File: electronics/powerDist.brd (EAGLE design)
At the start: 100 x 80 mm, 4 parts

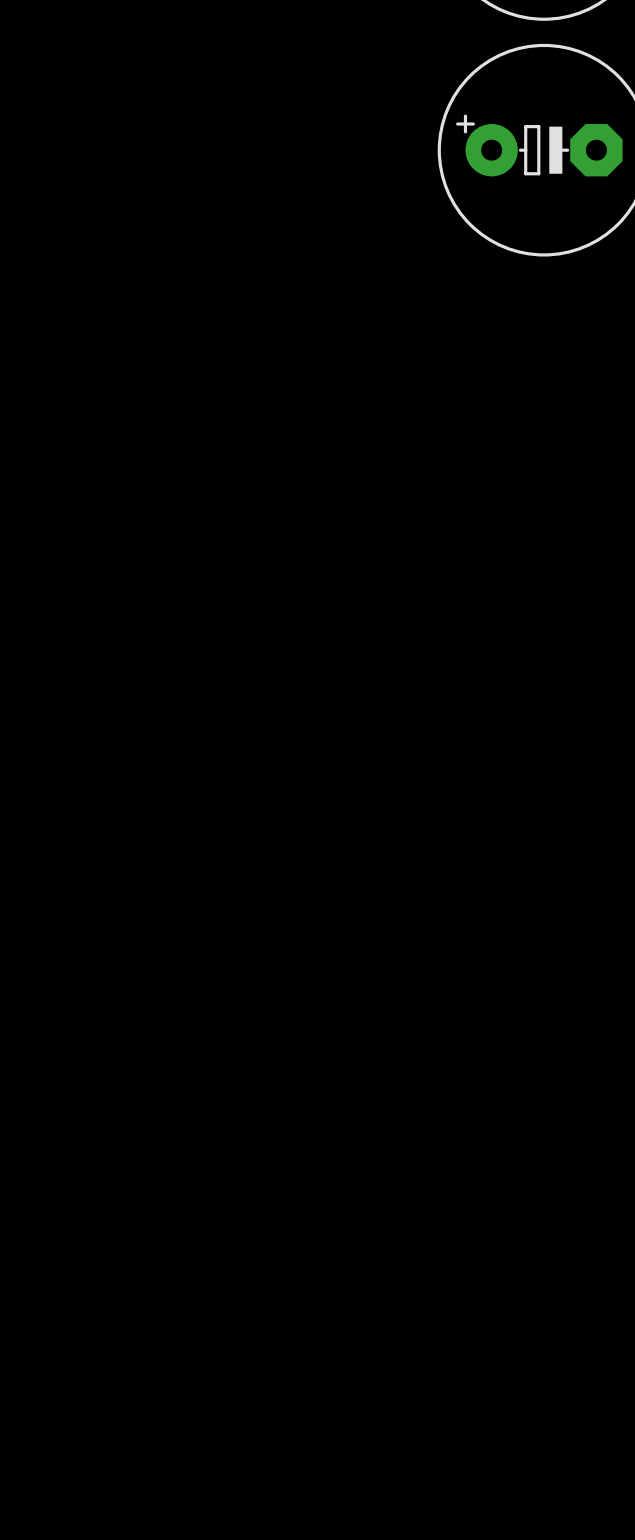
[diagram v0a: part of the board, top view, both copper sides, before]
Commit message: added msp430, went with drv ti motor drivers for galvos and brushed motor, max 1.8A
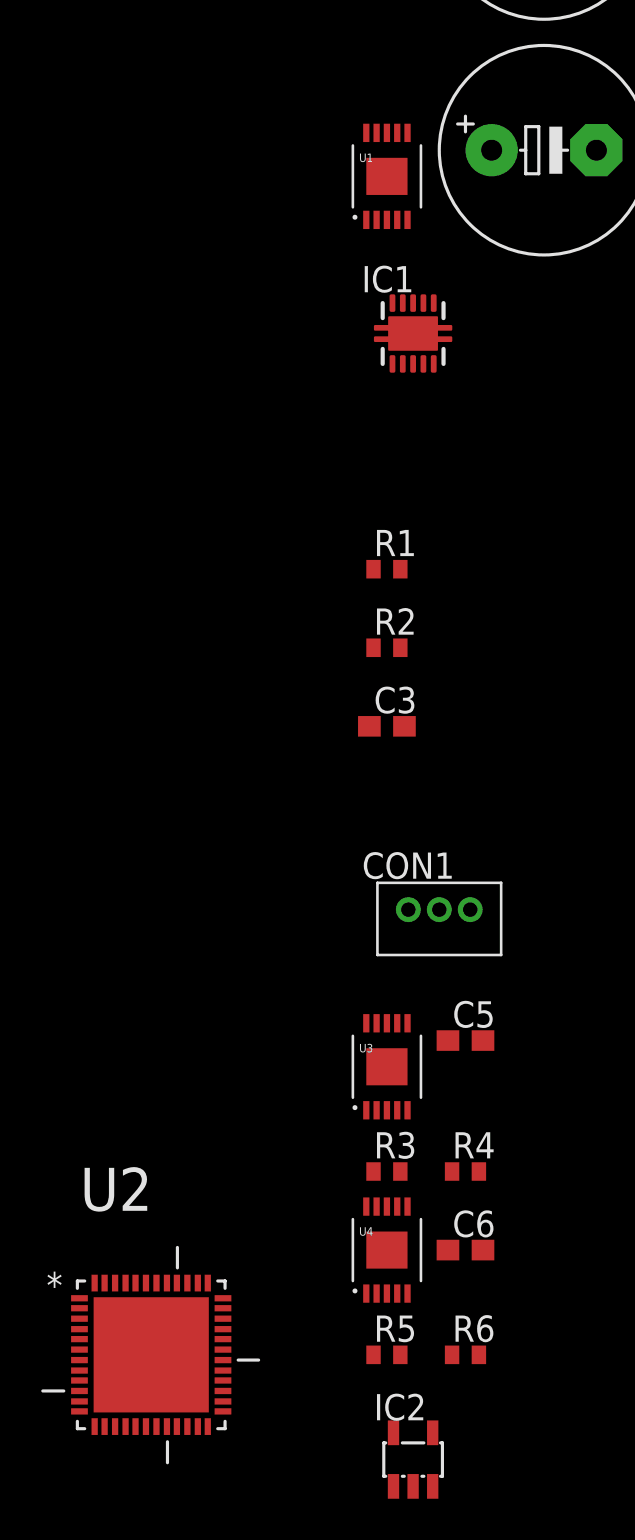
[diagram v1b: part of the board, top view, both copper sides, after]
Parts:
- added C3, C5, C6: (no value), rcl:C0603
- added CON1: B3B-ZR, jst:B3B-ZR
- added IC1: TPS6300, texas:DRC-S-PVSON-N10
- added IC2: TPS77033, texas:SOT23-DBV
- added R1, R2, R3, R4, R5, R6: (no value), rcl:R0402
- added U1, U3, U4: DRV8830, SparkFun-PowerIC:MSOP-10-GNDPAD
- added U2: MSP430F5500IRGZR, Texas Instruments_By_element14_Batch_1:QFN50P700X700X100-49N
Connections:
- new net +3V3: IC2.5
- new net +5V: C3.1, C5.1, C6.1, IC1.1, IC2.1, R1.2, R2.2, R3.2, R4.2, R5.2, R6.2, U1.4, U1.8, U3.4, U4.4, U4.7
- new net AVCC1: U2.7
- new net AVSS1: U2.10
- new net AVSS2: U2.44
- new net DRIVER_FAULT_1: U3.6
- new net DRIVER_FAULT_2: U4.6
- new net DRIVER_FAULT_3: U1.6
- new net DVCC1: U2.11
- new net DVCC2: U2.28
- new net DVSS1: U2.12
- new net DVSS2: U2.27
- new net MOTOR_SCL: R2.1, R4.1, R6.1, U1.10, U2.31, U3.10, U4.10
- new net MOTOR_SDA: R1.1, R3.1, R5.1, U1.9, U2.30, U3.9, U4.9
- new net OUT1: U1.3, U3.3, U4.3
- new net OUT2: U1.1, U3.1, U4.1
- new net PGND: IC1.3
- new net SAT_GND: CON1.2
- new net SAT_SERIAL: CON1.1, U2.34
- new net SAT_VCC: CON1.3
- new net V18: U2.43
- new net VCORE: U2.13
- new net VSSU: U2.37
- net GND: now also C3.2, C5.2, C6.2, IC1.9, IC2.2, IC2.3, U1.5, U1.7, U1.GND, U3.5, U3.7, U3.8, U3.GND, U4.5, U4.8, U4.GND

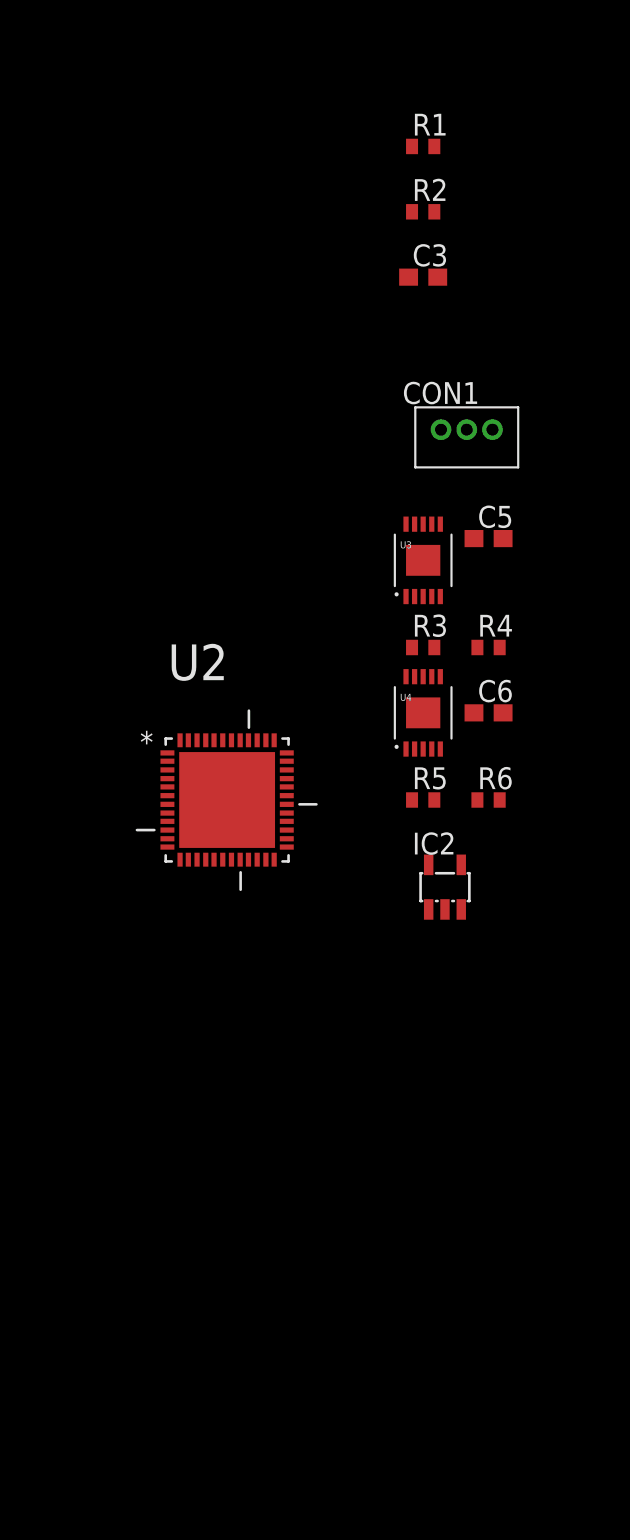
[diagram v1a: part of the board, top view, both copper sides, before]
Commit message: added passives to dc/dc.  todo figure out analog/micro stuff and connection points for motors
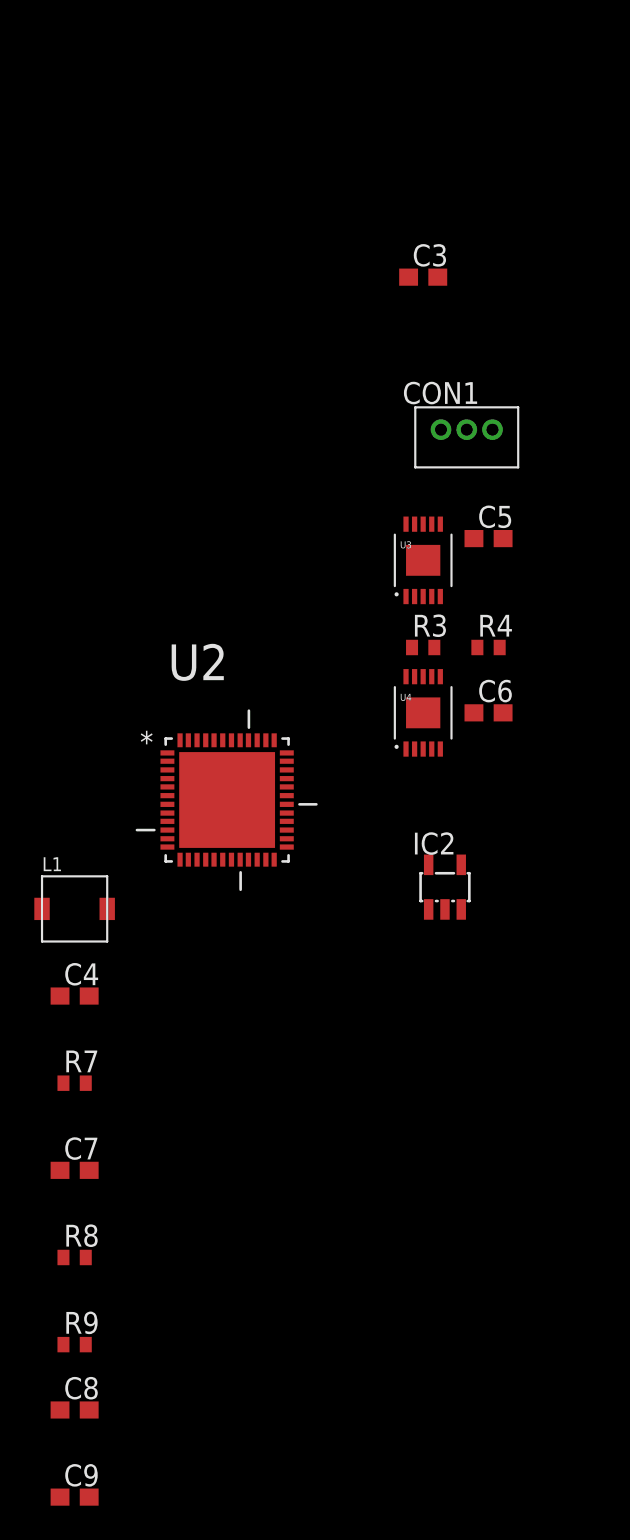
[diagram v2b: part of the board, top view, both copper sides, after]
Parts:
- removed R1, R2, R5, R6: (no value), rcl:R0402
- added C4: .1uf, rcl:C0603
- added C7, C8, C9: 10uf, rcl:C0603
- added L1: TDK-VLF4012AT-2R2M1R5, passives:TDK-VLF4012AT-2R2M1R5
- added R7: 100, rcl:R0402
- added R8, R9: (no value), rcl:R0402
- C3, C5, C6: value (none) -> .1uf
- R3, R4: value (none) -> 2k
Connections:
- removed net AVSS1: U2.10
- removed net AVSS2: U2.44
- removed net DVSS1: U2.12
- removed net DVSS2: U2.27
- removed net PGND: IC1.3
- removed net VSSU: U2.37
- new net N$3: IC1.4, L1.P$1
- new net N$4: IC1.2, L1.P$2
- new net N$8: C4.1, IC1.6, IC1.7, IC1.8, R7.1
- new net N$9: IC1.10, R8.1, R9.2
- net +5V: now also C8.1, C9.1, R8.2; no longer R1.2, R2.2, R5.2, R6.2
- net GND: now also C4.2, C7.2, C8.2, C9.2, IC1.3, R9.1, U2.10, U2.12, U2.27, U2.37, U2.44, U2.49
- net MOTOR_SCL: no longer R2.1, R6.1
- net MOTOR_SDA: no longer R1.1, R5.1
- net N$2: now also C7.1, IC1.5, R7.2

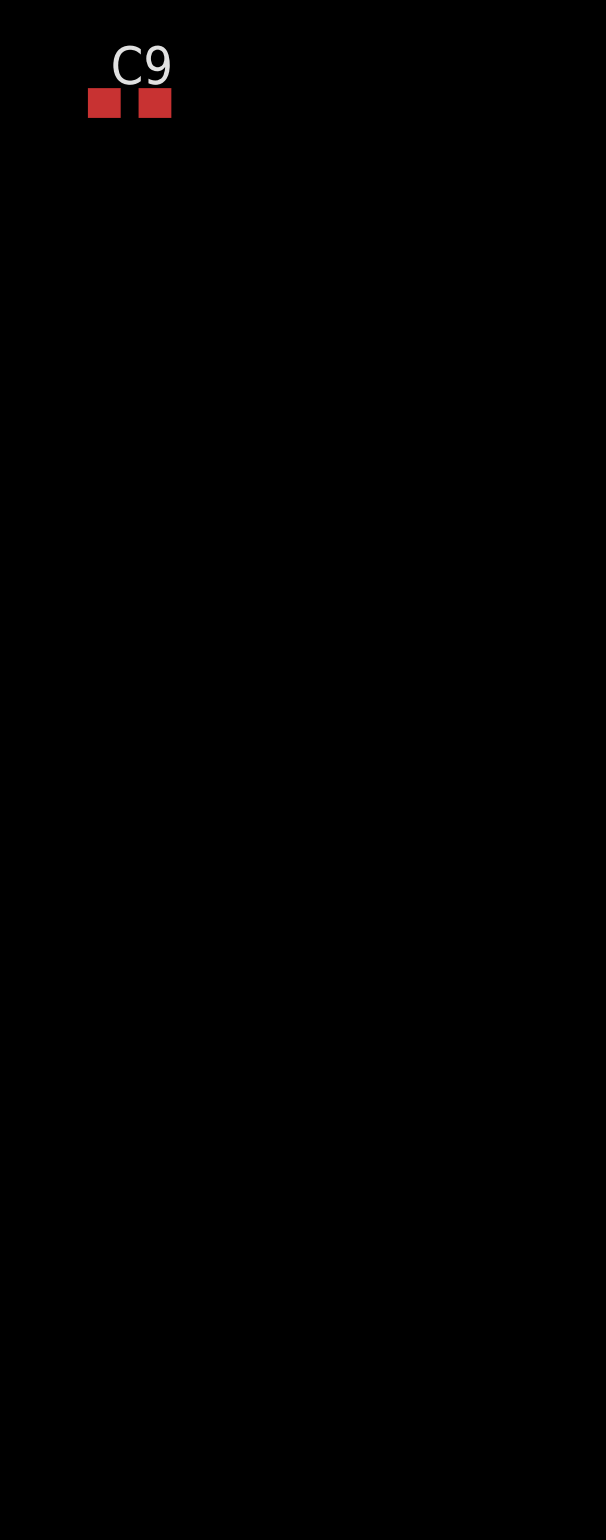
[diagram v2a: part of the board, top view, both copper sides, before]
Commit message: added decoupling to mcu
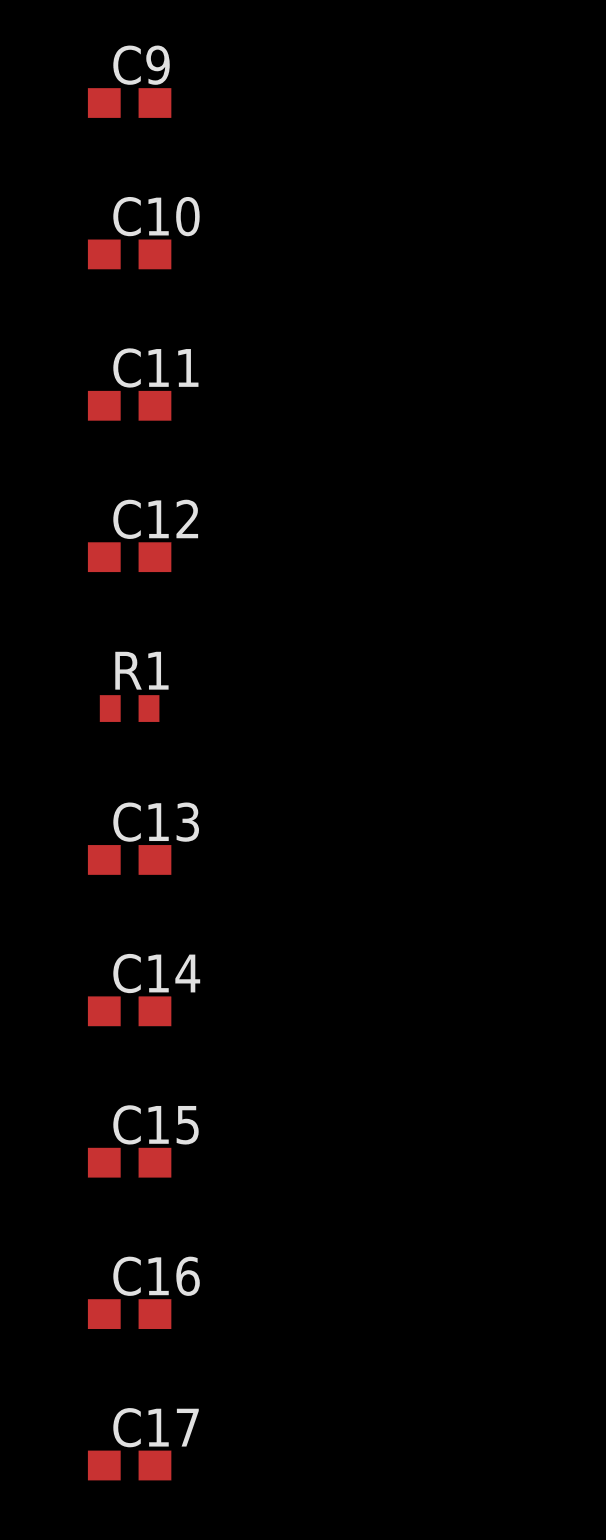
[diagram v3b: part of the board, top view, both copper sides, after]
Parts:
- added C10, C11, C12, C13: .1uf, rcl:C0603
- added C14, C15, C16, C17: 4.7uf, rcl:C0603
- added R1: 100, rcl:R0402
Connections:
- removed net AVCC1: U2.7
- removed net DVCC1: U2.11
- removed net DVCC2: U2.28
- removed net SAT_GND: CON1.2
- removed net SAT_VCC: CON1.3
- removed net VCORE: U2.13
- new net N$5: C13.1, C15.1, R1.2, U2.7
- new net N$7: C11.1, C14.1, U2.13
- net +3V3: now also C10.1, C12.1, C16.1, C17.1, CON1.3, R1.1, U2.11, U2.28
- net GND: now also C10.2, C11.2, C12.2, C13.2, C14.2, C15.2, C16.2, C17.2, CON1.2
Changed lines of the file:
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@@
 <element name="C8" library="rcl" package="C0603" value="10uf" x="-44.45" y="-111.76"/>
 <element name="C9" library="rcl" package="C0603" value="10uf" x="-44.45" y="-116.84"/>
+<element name="C10" library="rcl" package="C0603" value=".1uf" x="-44.45" y="-121.92"/>
+<element name="C11" library="rcl" package="C0603" value=".1uf" x="-44.45" y="-127"/>
+<element name="C12" library="rcl" package="C0603" value=".1uf" x="-44.45" y="-132.08"/>
+<element name="R1" library="rcl" package="R0402" value="100" x="-44.45" y="-137.16"/>
+<element name="C13" library="rcl" package="C0603" value=".1uf" x="-44.45" y="-142.24"/>
+<element name="C14" library="rcl" package="C0603" value="4.7uf" x="-44.45" y="-147.32"/>
+<element name="C15" library="rcl" package="C0603" value="4.7uf" x="-44.45" y="-152.4"/>
+<element name="C16" library="rcl" package="C0603" value="4.7uf" x="-44.45" y="-157.48"/>
+<element name="C17" library="rcl" package="C0603" value="4.7uf" x="-44.45" y="-162.56"/>
 </elements>
 <signals>
@@
 <contactref element="U2" pad="37"/>
 <contactref element="U2" pad="49"/>
+<contactref element="C11" pad="2"/>
+<contactref element="C10" pad="2"/>
+<contactref element="C12" pad="2"/>
+<contactref element="C13" pad="2"/>
+<contactref element="CON1" pad="2"/>
+<contactref element="C14" pad="2"/>
+<contactref element="C17" pad="2"/>
+<contactref element="C16" pad="2"/>
+<contactref element="C15" pad="2"/>
+<wire x1="-43.6" y1="-157.48" x2="-43.6" y2="-162.56" width="0" layer="19" extent="1-1"/>
+<wire x1="-43.6" y1="-152.4" x2="-43.6" y2="-157.48" width="0" layer="19" extent="1-1"/>
+<wire x1="-43.6" y1="-147.32" x2="-43.6" y2="-152.4" width="0" layer="19" extent="1-1"/>
+<wire x1="-43.6" y1="-142.24" x2="-43.6" y2="-147.32" width="0" layer="19" extent="1-1"/>
+<wire x1="-43.6" y1="-132.08" x2="-43.6" y2="-142.24" width="0" layer="19" extent="1-1"/>
+<wire x1="-43.6" y1="-127" x2="-43.6" y2="-132.08" width="0" layer="19" extent="1-1"/>
+<wire x1="-43.6" y1="-121.92" x2="-43.6" y2="-127" width="0" layer="19" extent="1-1"/>
+<wire x1="-43.6" y1="-116.84" x2="-43.6" y2="-121.92" width="0" layer="19" extent="1-1"/>
 <wire x1="-43.6" y1="-111.76" x2="-43.6" y2="-116.84" width="0" layer="19" extent="1-1"/>
 <wire x1="-45.1" y1="-107.95" x2="-43.6" y2="-111.76" width="0" layer="19" extent="1-1"/>
@@
 <wire x1="-23.63" y1="-60.1205" x2="-24.13" y2="-60.1205" width="0" layer="19" extent="1-1"/>
 <wire x1="-19.47" y1="-60.96" x2="-23.63" y2="-60.1205" width="0" layer="19" extent="1-1"/>
+<wire x1="-21.59" y1="-54.61" x2="-23.63" y2="-60.1205" width="0" layer="19" extent="1-1"/>
+<wire x1="-23.28" y1="-45.72" x2="-21.59" y2="-54.61" width="0" layer="19" extent="1-1"/>
 <wire x1="-22.86" y1="-82.58" x2="-23.13" y2="-73.2295" width="0" layer="19" extent="1-1"/>
 <wire x1="-21.91" y1="-82.58" x2="-22.86" y2="-82.58" width="0" layer="19" extent="1-1"/>
-<wire x1="-23.28" y1="-45.72" x2="-23.63" y2="-60.1205" width="0" layer="19" extent="1-1"/>
 <wire x1="-22.86" y1="-28.145" x2="-23.28" y2="-45.72" width="0" layer="19" extent="1-1"/>
 <wire x1="-23.36" y1="-25.195" x2="-22.86" y2="-28.145" width="0" layer="19" extent="1-1"/>
@@
 <wire x1="-24.63" y1="-16.9405" x2="-24.63" y2="-60.1205" width="0" layer="19" extent="1-1"/>
 </signal>
-<signal name="SAT_VCC">
-<contactref element="CON1" pad="3"/>
-</signal>
-<signal name="SAT_GND">
-<contactref element="CON1" pad="2"/>
-</signal>
 <signal name="SAT_SERIAL">
 <contactref element="CON1" pad="1"/>
@@
 <wire x1="-23.09" y1="-54.61" x2="-32.0802" y2="-74.4474" width="0" layer="19" extent="1-1"/>
 </signal>
-<signal name="AVCC1">
-<contactref element="U2" pad="7"/>
-</signal>
-<signal name="DVCC1">
-<contactref element="U2" pad="11"/>
-</signal>
-<signal name="DVCC2">
-<contactref element="U2" pad="28"/>
-</signal>
-<signal name="VCORE">
-<contactref element="U2" pad="13"/>
-</signal>
 <signal name="V18">
 <contactref element="U2" pad="43"/>
@@
 <signal name="+3V3">
 <contactref element="IC2" pad="5"/>
+<contactref element="U2" pad="11"/>
+<contactref element="C12" pad="1"/>
+<contactref element="U2" pad="28"/>
+<contactref element="C10" pad="1"/>
+<contactref element="R1" pad="1"/>
+<contactref element="CON1" pad="3"/>
+<contactref element="C17" pad="1"/>
+<contactref element="C16" pad="1"/>
+<wire x1="-45.3" y1="-157.48" x2="-45.3" y2="-162.56" width="0" layer="19" extent="1-1"/>
+<wire x1="-45.1" y1="-137.16" x2="-45.3" y2="-157.48" width="0" layer="19" extent="1-1"/>
+<wire x1="-45.3" y1="-132.08" x2="-45.1" y2="-137.16" width="0" layer="19" extent="1-1"/>
+<wire x1="-45.3" y1="-121.92" x2="-45.3" y2="-132.08" width="0" layer="19" extent="1-1"/>
+<wire x1="-39.0398" y1="-78.4606" x2="-45.3" y2="-121.92" width="0" layer="19" extent="1-1"/>
+<wire x1="-32.0802" y1="-77.4446" x2="-39.0398" y2="-78.4606" width="0" layer="19" extent="1-1"/>
+<wire x1="-23.81" y1="-79.98" x2="-32.0802" y2="-77.4446" width="0" layer="19" extent="1-1"/>
+<wire x1="-20.09" y1="-54.61" x2="-23.81" y2="-79.98" width="0" layer="19" extent="1-1"/>
 </signal>
 <signal name="N$3">
@@
 <wire x1="-23.86" y1="-25.195" x2="-45.1" y2="-102.87" width="0" layer="19" extent="1-1"/>
 </signal>
+<signal name="N$7">
+<contactref element="U2" pad="13"/>
+<contactref element="C11" pad="1"/>
+<contactref element="C14" pad="1"/>
+<wire x1="-45.3" y1="-127" x2="-45.3" y2="-147.32" width="0" layer="19" extent="1-1"/>
+<wire x1="-38.3032" y1="-79.6798" x2="-45.3" y2="-127" width="0" layer="19" extent="1-1"/>
+</signal>
+<signal name="N$5">
+<contactref element="U2" pad="7"/>
+<contactref element="R1" pad="2"/>
+<contactref element="C13" pad="1"/>
+<contactref element="C15" pad="1"/>
+<wire x1="-45.3" y1="-142.24" x2="-45.3" y2="-152.4" width="0" layer="19" extent="1-1"/>
+<wire x1="-43.8" y1="-137.16" x2="-45.3" y2="-142.24" width="0" layer="19" extent="1-1"/>
+<wire x1="-39.0398" y1="-76.454" x2="-43.8" y2="-137.16" width="0" layer="19" extent="1-1"/>
+</signal>
 </signals>

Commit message: arraning components for layout.  May move to 402 passives if it gets too crowded.
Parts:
- added C18: 4.7uf, rcl:C0603
- added C19, C22: .1uf, rcl:C0603
- added C20, C21: 18pf, rcl:C0603
- added J1, J2, J3, J4, J5, J6, J7, J8, J9: 2MMPAD, connectors:2MMPAD
- added R10, R11, R6: .22, rcl:R0402
- added R12, R5: 100, rcl:R0402
- added R2: 200k, rcl:R0402
- added U$1: 25Mhz, SparkFun-FreqCtrl:CRYSTAL-SMD-5X3
- R8: value (none) -> 1.8M
- R9: value (none) -> 200k
- moved C12 207.3 mm to (82.5, 31.8)
- moved C13 207.3 mm to (82.5, 21.6)
- moved C15 207.3 mm to (82.5, 11.4)
- moved C17 207.3 mm to (82.5, 1.27)
- moved C7 207.3 mm to (82.5, 66.0)
- moved C8 207.3 mm to (82.5, 52.1)
- moved C9 207.3 mm to (82.5, 47.0)
- moved R8 207.3 mm to (82.5, 61.0)
- moved R9 207.3 mm to (82.5, 55.9)
- moved C10 207.3 mm to (82.5, 41.9)
- moved C11 207.3 mm to (82.5, 36.8)
- moved C14 207.3 mm to (82.5, 16.5)
- moved C16 207.3 mm to (82.5, 6.35)
- moved C4 207.3 mm to (82.5, 76.2)
- moved R1 207.3 mm to (82.5, 26.7)
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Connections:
- removed net OUT1: U1.3, U3.3, U4.3
- removed net OUT2: U1.1, U3.1, U4.1
- new net N$10: J2.P$1, U4.1
- new net N$11: J3.P$1, U1.3
- new net N$12: J4.P$1, U1.1
- new net N$13: J5.P$1, U3.3
- new net N$14: J6.P$1, U3.1
- new net N$15: C20.1, U$1.1, U2.45
- new net N$16: C21.1, U$1.3, U2.46
- new net N$17: R6.2, U1.2
- new net N$18: R11.2, U3.2
- new net N$19: R10.2, U4.2
- new net N$20: C22.1, R12.2, U2.5
- new net N$6: J1.P$1, U4.3
- new net VSUPP_FEEDBACK: C18.1, C19.1, R2.1, R5.1, U2.1
- net +3V3: now also R12.1
- net FROM_PANNEL_1: now also J8.P$1
- net FROM_PANNEL_2: now also J7.P$1
- net GND: now also C18.2, C19.2, C20.2, C21.2, C22.2, J9.P$1, R10.1, R11.1, R5.2, R6.1, U$1.2, U$1.4, U2.6
- net N$2: now also R2.2
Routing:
- added copper zone on layer 1, net +3V3
- added copper zone on layer 16, net GND
